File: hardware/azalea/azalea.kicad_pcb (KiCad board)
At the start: 4 copper layers, 70.6 x 53.3 mm, 88 parts, among them J1 NEIGHBOR1, J2 NEIGHBOR2, J3 USB-MICRO-B-SHIELDED, J4 USB-MICRO-B-SHIELDED, J5 JTAG, J7 BONUS_ROW, SW1 DFU, SW2 RESET, U1 LPC4330FBD144, U2 W25Q16DV, U3 AP7333, U4 IP4220CZ6, U5 NX5P2553GV, X1 XTAL4PIN, X2 RTC_XTAL

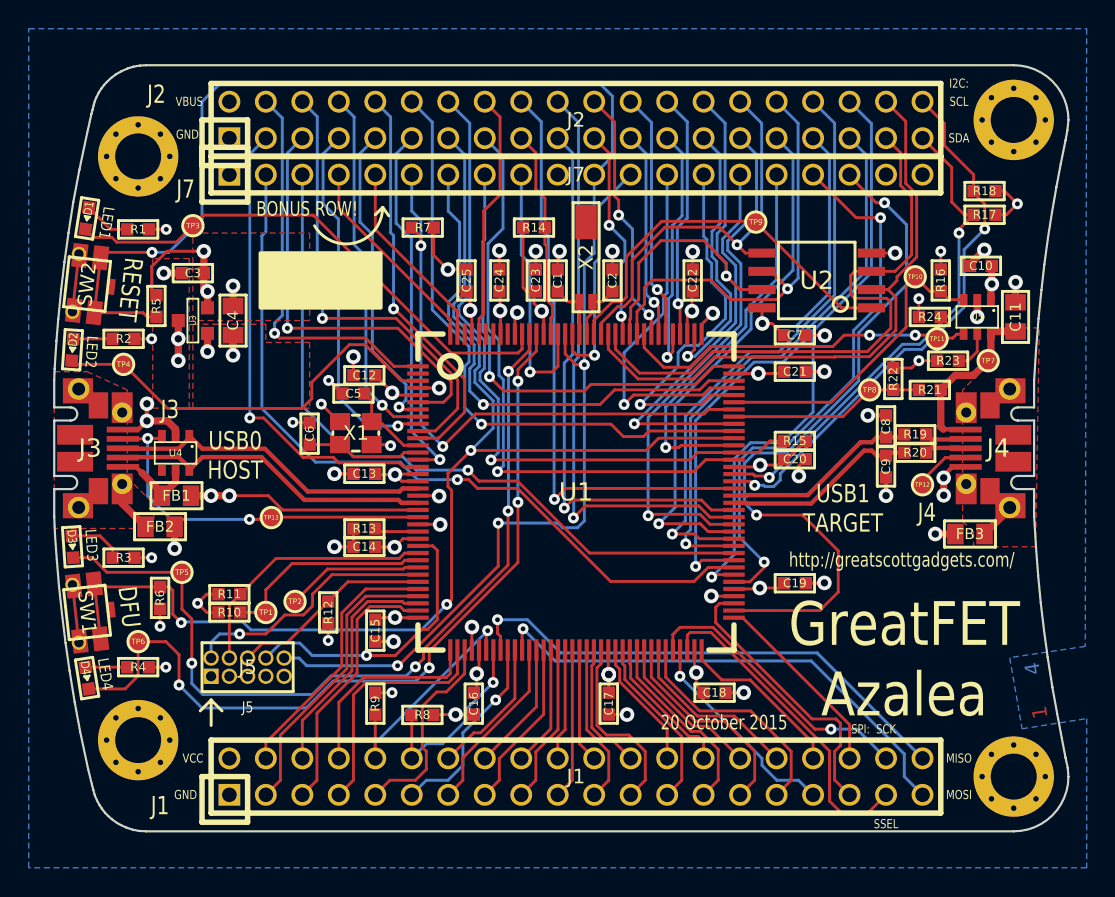
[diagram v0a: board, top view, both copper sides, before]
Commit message: azalea: nudged some 0402s that did not need to be so close together
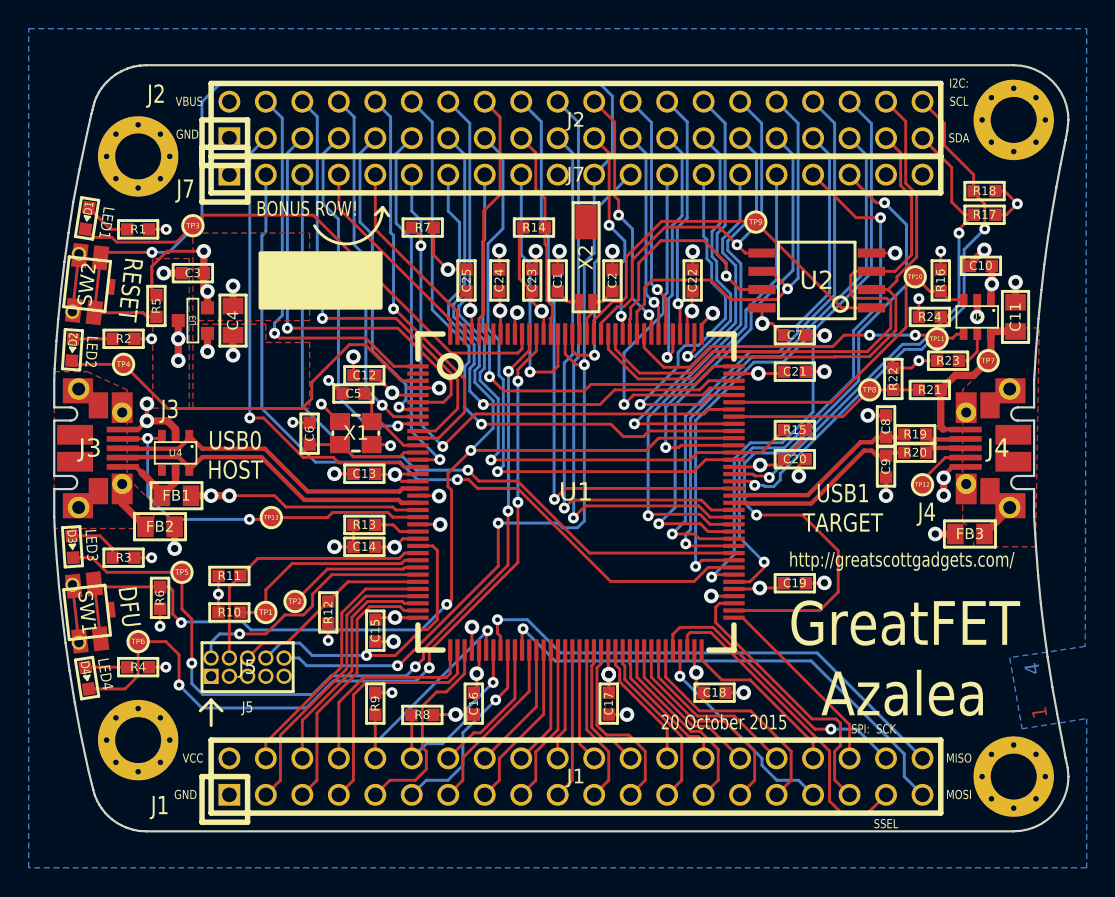
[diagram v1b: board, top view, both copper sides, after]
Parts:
- moved R11 1.27 mm to (118.1, 106.7)
- moved R15 0.76 mm to (157.5, 96.5)
- moved R13 0.25 mm to (127.5, 103.1)
- moved C23 0.25 mm to (139.2, 86.1)
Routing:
- net /TCK: track 18.3 -> 19.1 mm
- net VCC: track 87.4 -> 86.9 mm

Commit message: extended crystal pads for easier soldering
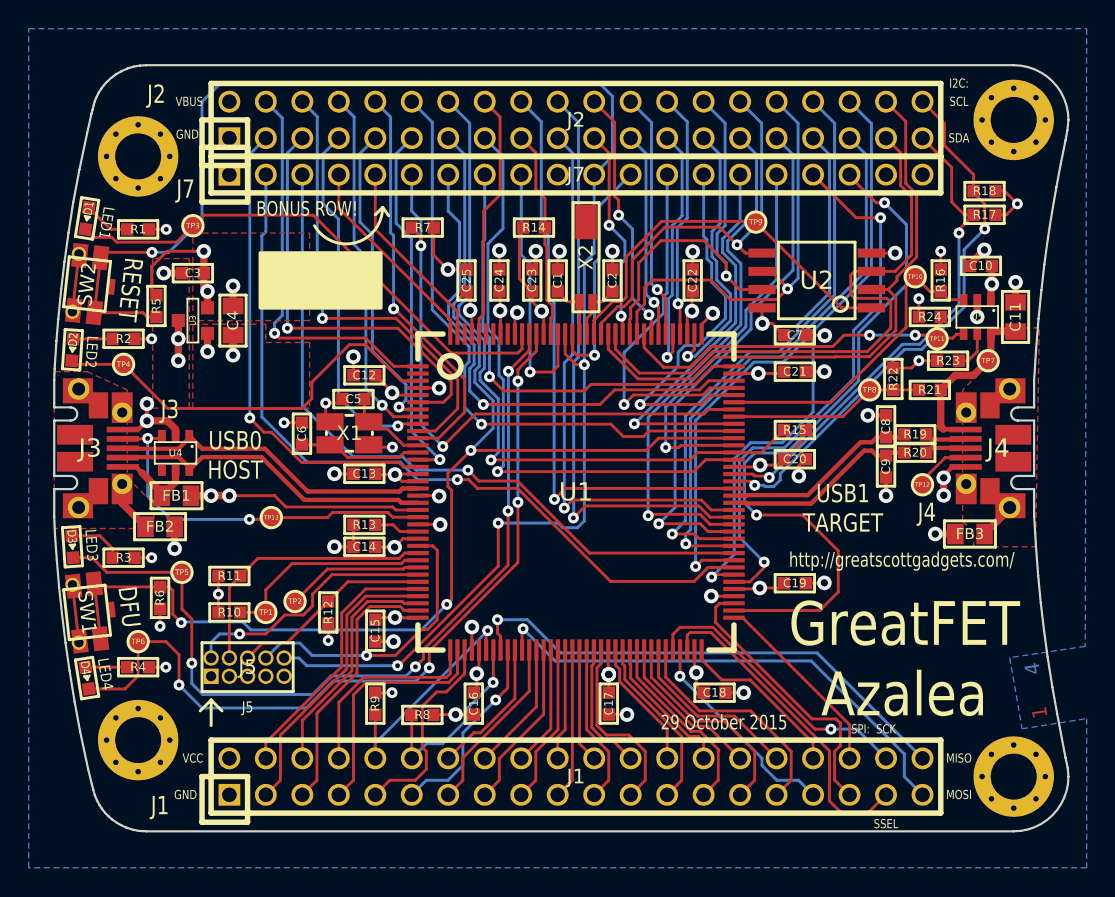
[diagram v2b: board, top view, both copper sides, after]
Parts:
- X1: footprint gsg-modules:XTAL3.2x2.5mm -> gsg-modules:XTAL3.2x2.5mm-EXT
- moved C6 0.53 mm to (123.2, 96.8)
- moved X1 0.45 mm to (126.5, 96.7)
- moved C5 0.38 mm to (126.7, 94.4)
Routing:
- net Net-(C6-Pad1): track 8.02 -> 8.57 mm
- net GND: vias 47 -> 46
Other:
- board text added: "29 October 2015"
- board text removed: "20 October 2015"

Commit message: azalea: corrected value of 47 pF caps that were changed to 18 pF
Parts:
- C8, C9: value 47pF -> 18pF
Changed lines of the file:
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@@
     (links 352)
     (no_connects 0)
-    (area 93.271704 68.58 275.715801 199.465001)
+    (area 105.842999 71.044999 176.605001 124.535001)
     (thickness 1.6)
     (drawings 146)
@@
       (effects (font (size 0.6096 0.6096) (thickness 0.1524)))
     )
-    (fp_text value 47pF (at 0 0 90) (layer F.SilkS) hide
+    (fp_text value 18pF (at 0 0 90) (layer F.SilkS) hide
       (effects (font (size 0.6096 0.6096) (thickness 0.1524)))
     )
@@
       (effects (font (size 0.6096 0.6096) (thickness 0.1524)))
     )
-    (fp_text value 47pF (at 0 0 270) (layer F.SilkS) hide
-      (effects (font (size 0.6096 0.6096) (thickness 0.1524)))
-    )
+    (fp_text value 18pF (at 0 0 270) (layer F.SilkS) hide
+      (effects (font (size 0.6096 0.6096) (thickness 0.1524)))
+    )

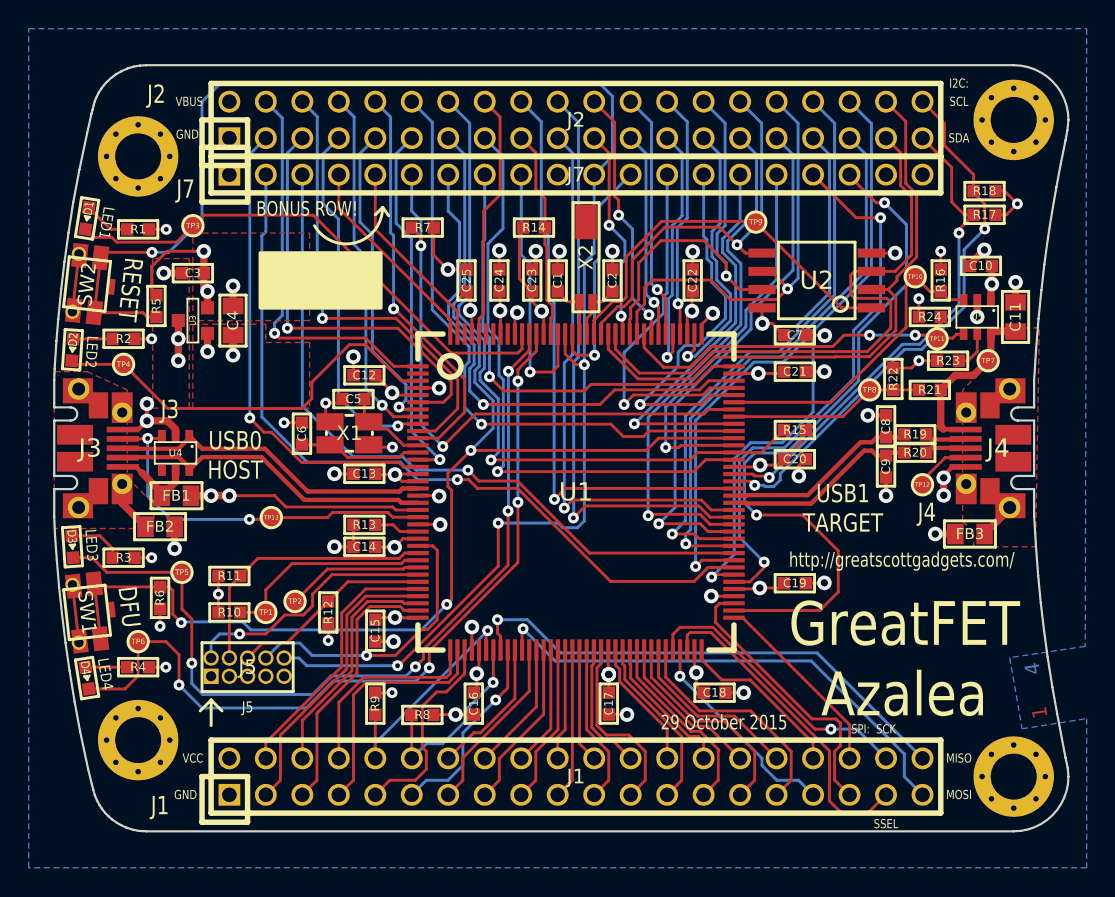
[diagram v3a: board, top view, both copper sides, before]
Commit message: azalea: moved layer legend
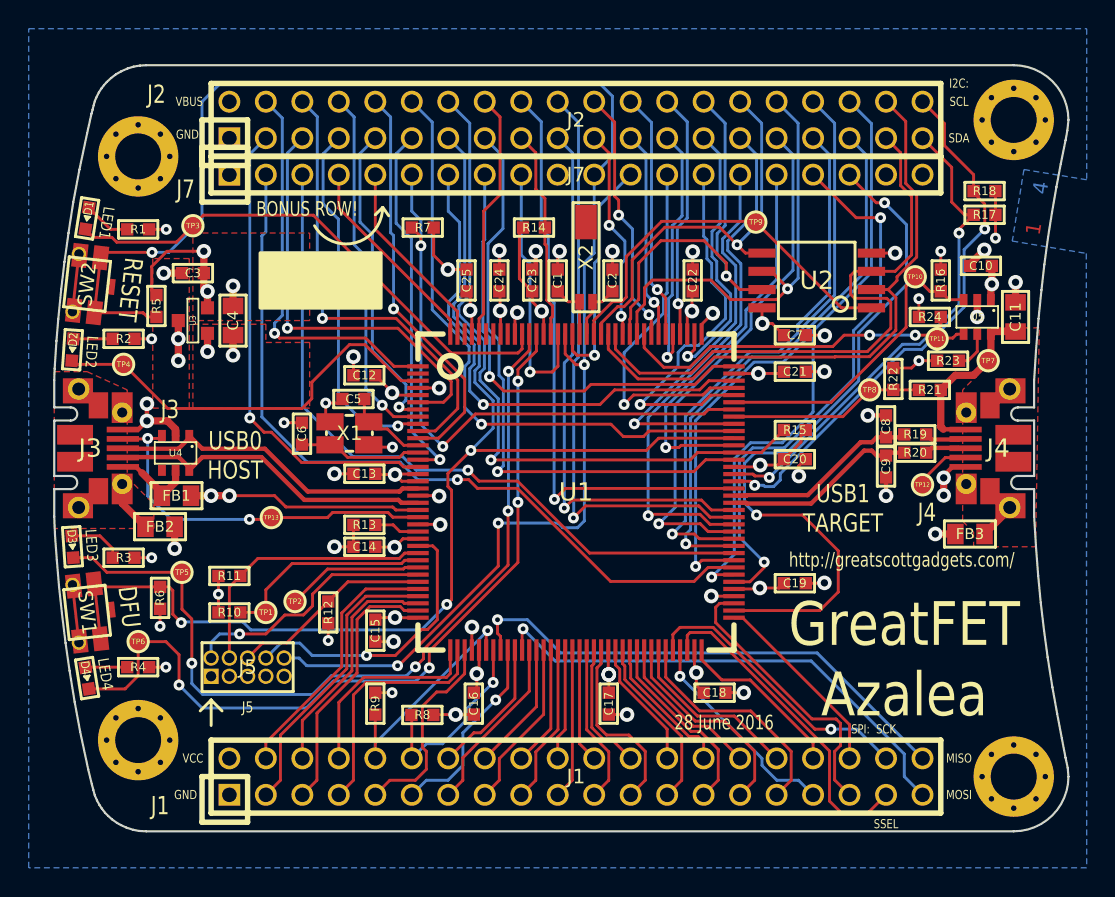
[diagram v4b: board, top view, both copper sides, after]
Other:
- board text added: "28 June 2016"
- board text removed: "29 October 2015"
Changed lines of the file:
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@@
     (links 352)
     (no_connects 0)
-    (area 105.842999 71.044999 176.605001 124.535001)
+    (area 93.271704 68.58 275.715801 199.465001)
     (thickness 1.6)
     (drawings 146)
-    (tracks 1431)
+    (tracks 1432)
     (zones 0)
     (modules 88)
@@
       (net 1 GND))
   )
-  (gr_text 4 (at 174.0408 113.1316 98.9) (layer B.Cu)
+  (gr_text 4 (at 174.5996 79.6544 80.5) (layer B.Cu)
     (effects (font (size 1.016 1.016) (thickness 0.1778)))
   )
-  (gr_text 3 (at 174.2186 114.173 98.9) (layer C3.Cu)
+  (gr_text 3 (at 174.4218 80.5942 80.5) (layer C3.Cu)
     (effects (font (size 1.016 1.016) (thickness 0.1778)))
   )
-  (gr_text 2 (at 174.371 115.1636 98.9) (layer C2.Cu)
+  (gr_text 2 (at 174.2694 81.5594 80.5) (layer C2.Cu)
     (effects (font (size 1.016 1.016) (thickness 0.1778)))
   )
-  (gr_text 1 (at 174.5488 116.1796 98.9) (layer F.Cu)
+  (gr_text 1 (at 174.117 82.4992 80.5) (layer F.Cu)
     (effects (font (size 1.016 1.016) (thickness 0.1778)))
   )
@@
   (gr_line (start 128.778 81.026) (end 128.27 81.534) (angle 90) (layer F.SilkS) (width 0.15))
   (gr_arc (start 126.238 81.026) (end 128.778 81.026) (angle 150) (layer F.SilkS) (width 0.2032))
-  (gr_text "29 October 2015" (at 152.5524 116.8908) (layer F.SilkS)
+  (gr_text "28 June 2016" (at 152.5524 116.8908) (layer F.SilkS)
     (effects (font (size 1.016 0.762) (thickness 0.1524)))
   )
@@
   (gr_line (start 116.84 115.316) (end 117.602 116.078) (layer F.SilkS) (width 0.2032))
   (gr_line (start 116.84 115.316) (end 116.078 116.078) (layer F.SilkS) (width 0.2032))
-  (gr_arc (start 275.6408 97.79) (end 174.0408 97.79) (angle 12.5) (layer Cmts.User) (width 0.15))
+  (gr_arc (start 267.0556 116.8908) (end 165.4556 116.8908) (angle 12.5) (layer Cmts.User) (width 0.15))
   (gr_text "GreatFET\nAzalea" (at 165.1 112.522) (layer F.SilkS)
     (effects (font (size 3.048 2.54) (thickness 0.4572)))
@@
   (gr_arc (start 207.391 97.79) (end 105.791 97.79) (angle -13.2) (layer Cmts.User) (width 0.15))
   (gr_arc (start 207.391 97.79) (end 105.791 97.79) (angle 13.2) (layer Cmts.User) (width 0.15))
-  (gr_arc (start 275.6408 97.79) (end 174.0408 97.79) (angle -12.5) (layer Cmts.User) (width 0.15))
+  (gr_arc (start 267.0556 116.8908) (end 165.4556 116.8908) (angle -12.5) (layer Cmts.User) (width 0.15))
   (gr_circle (center 111.76 118.11) (end 111.76 121.92) (layer Cmts.User) (width 0.2032))
   (gr_circle (center 111.76 77.47) (end 111.76 73.66) (layer Cmts.User) (width 0.2032))
@@
   (segment (start 142.48892 89.83726) (end 142.48892 87.59708) (width 0.2032) (layer F.Cu) (net 3) (status 30))
   (segment (start 142.48892 87.59708) (end 142.494 87.592) (width 0.2032) (layer F.Cu) (net 3) (status 30))
+  (segment (start 171.45 81.534) (end 171.45 83.1596) (width 0.2032) (layer F.Cu) (net 4))
+  (via (at 171.45 83.1596) (size 0.762) (drill 0.3302) (layers F.Cu B.Cu) (net 4))
+  (segment (start 171.45 79.883) (end 171.45 81.534) (width 0.2032) (layer F.Cu) (net 4))
+  (segment (start 171.45 81.534) (end 171.4754 81.5594) (width 0.2032) (layer F.Cu) (net 4))
+  (segment (start 171.4754 81.5594) (end 171.5516 81.5594) (width 0.2032) (layer F.Cu) (net 4))
+  (segment (start 171.5516 81.5594) (end 171.45 81.534) (width 0.2032) (layer F.Cu) (net 4))
   (segment (start 139.192 86.868) (end 138.303 85.979) (width 0.2032) (layer F.Cu) (net 4))
   (segment (start 138.303 85.979) (end 138.303 82.677) (width 0.2032) (layer F.Cu) (net 4))
@@
   (segment (start 130.2004 104.0892) (end 129.6162 104.6734) (width 0.2032) (layer F.Cu) (net 4))
   (via (at 129.6162 104.6734) (size 1.016) (drill 0.508) (layers F.Cu B.Cu) (net 4))
-  (segment (start 171.45 81.534) (end 172.212 81.534) (width 0.2032) (layer F.Cu) (net 4) (status 10))
-  (segment (start 172.212 81.534) (end 172.974 80.772) (width 0.2032) (layer F.Cu) (net 4))
-  (segment (start 171.45 79.883) (end 172.085 79.883) (width 0.2032) (layer F.Cu) (net 4) (status 10))
-  (segment (start 172.085 79.883) (end 172.974 80.772) (width 0.2032) (layer F.Cu) (net 4))
-  (via (at 172.974 80.772) (size 0.762) (drill 0.3302) (layers F.Cu B.Cu) (net 4))
   (segment (start 154.94 92.583) (end 156.591 92.583) (width 0.2032) (layer F.Cu) (net 4) (status 20))
   (segment (start 156.591 92.583) (end 156.718 92.456) (width 0.2032) (layer F.Cu) (net 4) (status 30))
@@
     (polygon
       (pts
-        (xy 104.14 68.58) (xy 177.8 68.58) (xy 177.6984 111.5822) (xy 172.4406 112.3696) (xy 173.3042 117.3226)
-        (xy 177.8254 116.6114) (xy 177.8 127) (xy 104.14 127)
+        (xy 104.14 68.58) (xy 177.8 68.58) (xy 177.8 79.0956) (xy 173.4312 78.3844) (xy 172.6184 83.3628)
+        (xy 177.7746 84.2264) (xy 177.8 127) (xy 104.14 127)
       )
     )
@@
     (polygon
       (pts
-        (xy 104.14 68.58) (xy 177.8 68.58) (xy 177.6984 111.5822) (xy 172.4406 112.3696) (xy 173.3042 117.3226)
-        (xy 177.8 116.6114) (xy 177.8 127) (xy 104.14 127)
+        (xy 104.14 68.58) (xy 177.8 68.58) (xy 177.8 79.0956) (xy 173.4312 78.3844) (xy 172.6184 83.3628)
+        (xy 177.7746 84.2264) (xy 177.8 127) (xy 104.14 127)
       )
     )
@@
     (polygon
       (pts
-        (xy 104.14 68.58) (xy 177.8 68.58) (xy 177.6984 111.5822) (xy 172.4406 112.3696) (xy 173.3042 117.3226)
-        (xy 177.8 116.6114) (xy 177.8 127) (xy 104.14 127)
+        (xy 104.14 68.58) (xy 177.8 68.58) (xy 177.8 79.0956) (xy 173.4312 78.3844) (xy 172.6184 83.3628)
+        (xy 177.7746 84.2264) (xy 177.8 127) (xy 104.14 127)
       )
     )
